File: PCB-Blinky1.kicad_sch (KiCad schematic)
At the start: 1 part, among them U1 STM32F411CEU6

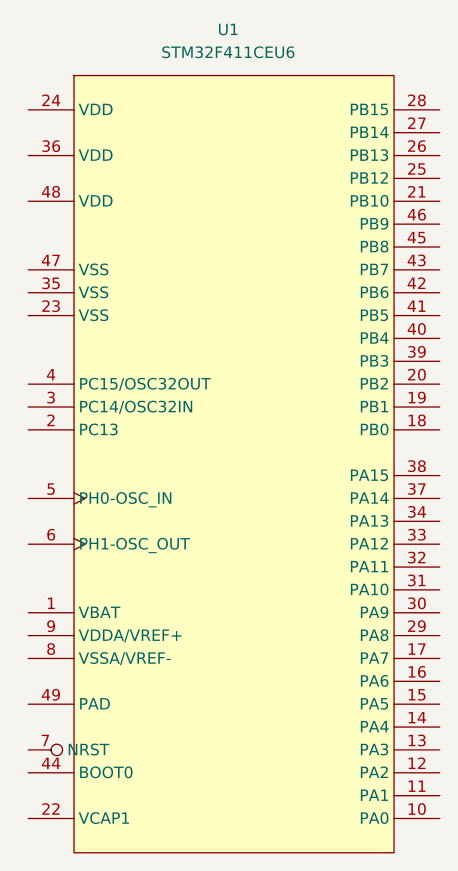
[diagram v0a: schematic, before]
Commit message: LED added
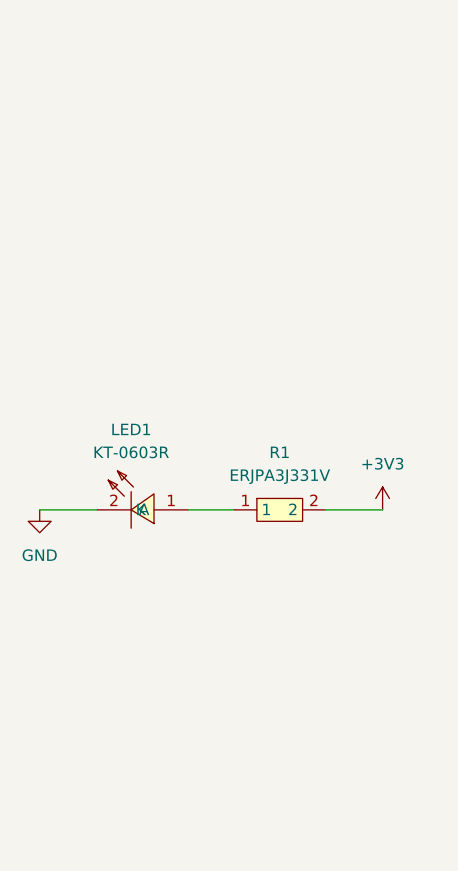
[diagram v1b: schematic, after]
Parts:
- removed U1: STM32F411CEU6, EasyEDA:UFQFPN-48_L7.0-W7.0-P0.50-BL-EP, symbol EasyEDA:STM32F411CEU6
- added LED1: KT-0603R, EasyEDA:LED-SMD_L1.6-W0.8-R-RD, symbol EasyEDA:KT-0603R
- added R1: ERJPA3J331V, EasyEDA:R0603, symbol EasyEDA:ERJPA3J331V
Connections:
- new net: LED1.1 (A), R1.1
- new net +3V3: R1.2
- new net GND: LED1.2 (K)
